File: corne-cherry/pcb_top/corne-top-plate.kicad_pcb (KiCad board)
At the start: 2 copper layers, 151.9 x 91.4 mm, 5 parts

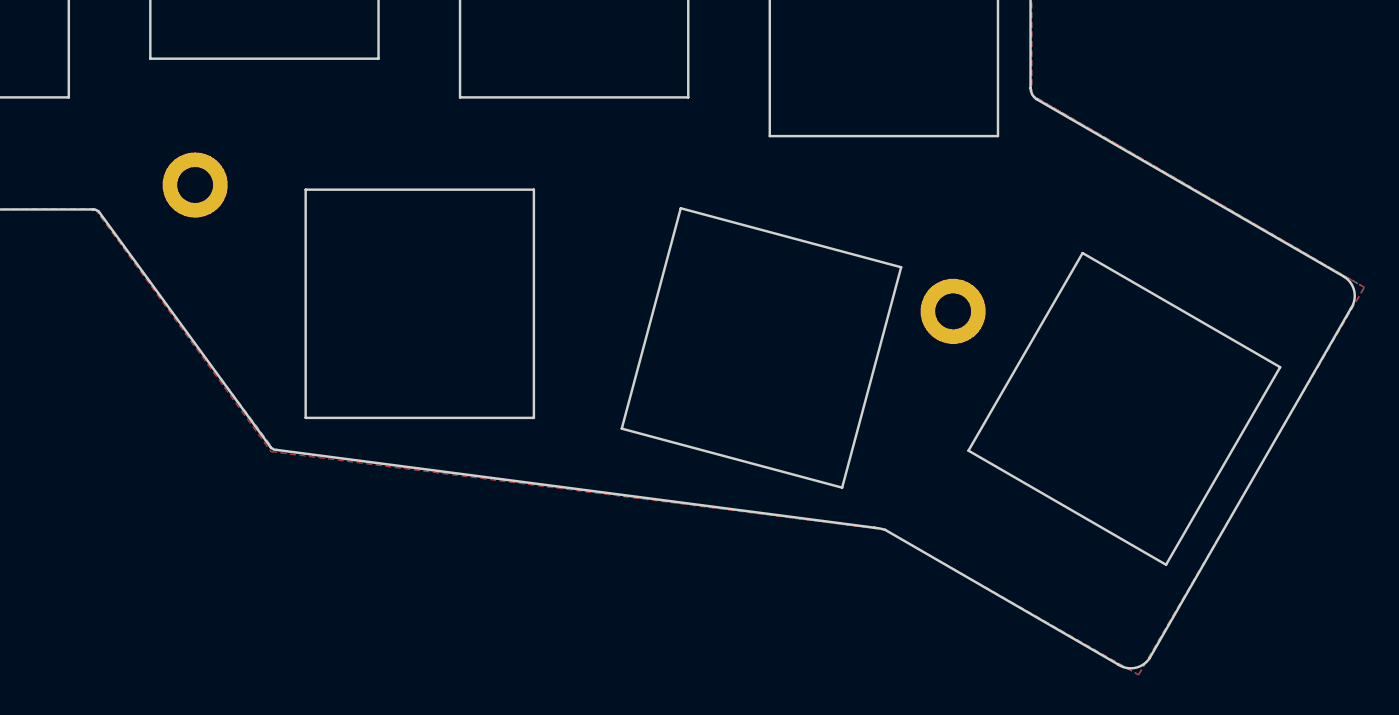
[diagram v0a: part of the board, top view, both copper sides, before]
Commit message: fixed outlines for pcb plates
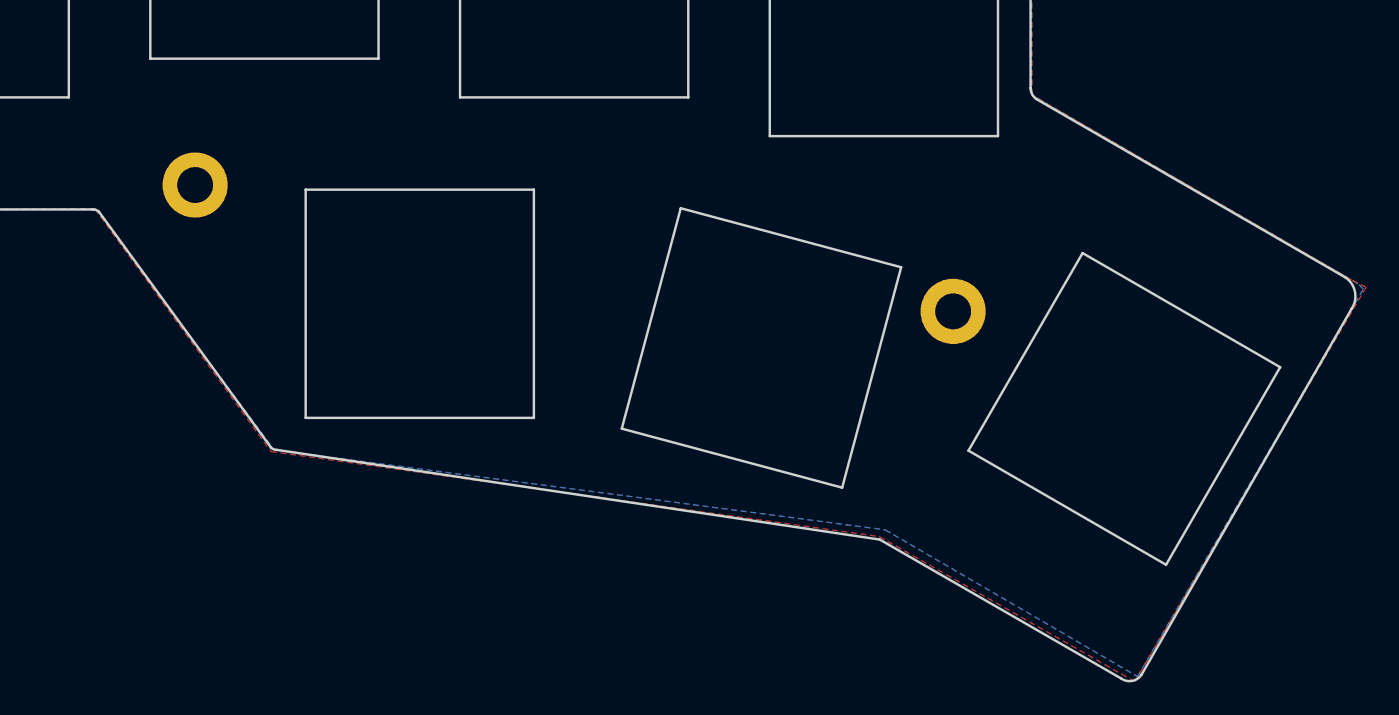
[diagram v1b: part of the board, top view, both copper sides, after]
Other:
- board size 151.9 x 91.4 mm -> 152 x 92.2 mm
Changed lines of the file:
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@@
-(kicad_pcb (version 20171130) (host pcbnew "(5.1.0)-1")
+(kicad_pcb (version 20171130) (host pcbnew "(5.1.8)-1")
   (general
     (thickness 1.6)
-    (drawings 137)
+    (drawings 136)
     (tracks 0)
     (zones 0)
@@
       (effects (font (size 1 1) (thickness 0.15)))
     )
-    (fp_text user %R (at 0.3 0) (layer F.Fab)
-      (effects (font (size 1 1) (thickness 0.15)))
-    )
-    (fp_circle (center 0 0) (end 2.2 0) (layer Cmts.User) (width 0.15))
-    (fp_circle (center 0 0) (end 2.45 0) (layer F.CrtYd) (width 0.05))
+    (fp_circle (center 0 0) (end 2.2 0) (layer Cmts.User) (width 0.15))
+    (fp_circle (center 0 0) (end 2.45 0) (layer F.CrtYd) (width 0.05))
+    (fp_text user %R (at 0.3 0) (layer F.Fab)
+      (effects (font (size 1 1) (thickness 0.15)))
+    )
     (pad "" thru_hole circle (at 0 0) (size 4 4) (drill 2.2) (layers *.Cu *.Mask))
   )
@@
       (effects (font (size 1 1) (thickness 0.15)))
     )
-    (fp_text user %R (at 0.3 0) (layer F.Fab)
-      (effects (font (size 1 1) (thickness 0.15)))
-    )
-    (fp_circle (center 0 0) (end 2.2 0) (layer Cmts.User) (width 0.15))
-    (fp_circle (center 0 0) (end 2.45 0) (layer F.CrtYd) (width 0.05))
+    (fp_circle (center 0 0) (end 2.2 0) (layer Cmts.User) (width 0.15))
+    (fp_circle (center 0 0) (end 2.45 0) (layer F.CrtYd) (width 0.05))
+    (fp_text user %R (at 0.3 0) (layer F.Fab)
+      (effects (font (size 1 1) (thickness 0.15)))
+    )
     (pad "" thru_hole circle (at 0 0) (size 4 4) (drill 2.2) (layers *.Cu *.Mask))
   )
@@
       (effects (font (size 1 1) (thickness 0.15)))
     )
-    (fp_text user %R (at 0.3 0) (layer F.Fab)
-      (effects (font (size 1 1) (thickness 0.15)))
-    )
-    (fp_circle (center 0 0) (end 2.2 0) (layer Cmts.User) (width 0.15))
-    (fp_circle (center 0 0) (end 2.45 0) (layer F.CrtYd) (width 0.05))
+    (fp_circle (center 0 0) (end 2.2 0) (layer Cmts.User) (width 0.15))
+    (fp_circle (center 0 0) (end 2.45 0) (layer F.CrtYd) (width 0.05))
+    (fp_text user %R (at 0.3 0) (layer F.Fab)
+      (effects (font (size 1 1) (thickness 0.15)))
+    )
     (pad "" thru_hole circle (at 0 0) (size 4 4) (drill 2.2) (layers *.Cu *.Mask))
   )
@@
       (effects (font (size 1 1) (thickness 0.15)))
     )
-    (fp_text user %R (at 0.3 0) (layer F.Fab)
-      (effects (font (size 1 1) (thickness 0.15)))
-    )
-    (fp_circle (center 0 0) (end 2.2 0) (layer Cmts.User) (width 0.15))
-    (fp_circle (center 0 0) (end 2.45 0) (layer F.CrtYd) (width 0.05))
+    (fp_circle (center 0 0) (end 2.2 0) (layer Cmts.User) (width 0.15))
+    (fp_circle (center 0 0) (end 2.45 0) (layer F.CrtYd) (width 0.05))
+    (fp_text user %R (at 0.3 0) (layer F.Fab)
+      (effects (font (size 1 1) (thickness 0.15)))
+    )
     (pad "" thru_hole circle (at 0 0) (size 4 4) (drill 2.2) (layers *.Cu *.Mask))
   )
@@
       (effects (font (size 1 1) (thickness 0.15)))
     )
-    (fp_text user %R (at 0.3 0) (layer F.Fab)
-      (effects (font (size 1 1) (thickness 0.15)))
-    )
-    (fp_circle (center 0 0) (end 2.2 0) (layer Cmts.User) (width 0.15))
-    (fp_circle (center 0 0) (end 2.45 0) (layer F.CrtYd) (width 0.05))
-    (pad "" thru_hole circle (at 0 0) (size 4 4) (drill 2.2) (layers *.Cu *.Mask))
-  )
+    (fp_circle (center 0 0) (end 2.2 0) (layer Cmts.User) (width 0.15))
+    (fp_circle (center 0 0) (end 2.45 0) (layer F.CrtYd) (width 0.05))
+    (fp_text user %R (at 0.3 0) (layer F.Fab)
+      (effects (font (size 1 1) (thickness 0.15)))
+    )
+    (pad "" thru_hole circle (at 0 0) (size 4 4) (drill 2.2) (layers *.Cu *.Mask))
+  )
+  (gr_line (start 180.8 152.8) (end 193.68968 130.34646) (angle 90) (layer Edge.Cuts) (width 0.15))
   (gr_line (start 44 98.375) (end 44 84.375) (layer Edge.Cuts) (width 0.15))
   (gr_line (start 44 98.375) (end 58 98.375) (layer Edge.Cuts) (width 0.15))
@@
   (gr_line (start 63 70.125) (end 77 70.125) (layer Edge.Cuts) (width 0.15))
   (gr_arc (start 174.847282 116.785192) (end 173.997282 116.810192) (angle -52.52752939) (layer Edge.Cuts) (width 0.15))
-  (gr_arc (start 192.500001 129.550001) (end 193.65 130.325) (angle -90.22347501) (layer Edge.Cuts) (width 0.15))
-  (gr_line (start 193.270509 128.396988) (end 174.35 117.475) (layer Edge.Cuts) (width 0.15))
+  (gr_arc (start 192.539681 129.571461) (end 193.68968 130.34646) (angle -90.22347501) (layer Edge.Cuts) (width 0.15))
+  (gr_line (start 193.310189 128.418448) (end 174.35 117.475) (layer Edge.Cuts) (width 0.15))
   (gr_line (start 63 84.125) (end 63 70.125) (layer Edge.Cuts) (width 0.15))
   (gr_line (start 77 70.125) (end 77 84.125) (layer Edge.Cuts) (width 0.15))
-  (gr_arc (start 180.14425 151.010957) (end 179.369251 152.160956) (angle -90.22347501) (layer Edge.Cuts) (width 0.15))
-  (gr_arc (start 164.087404 147.16844) (end 165.075 143.9) (angle -11.21335546) (layer Edge.Cuts) (width 0.15))
-  (gr_line (start 181.297263 151.781465) (end 193.65 130.325) (layer Edge.Cuts) (width 0.15))
-  (gr_line (start 165.075 143.9) (end 179.369251 152.160956) (layer Edge.Cuts) (width 0.15))
-  (gr_line (start 127.75 139) (end 164.420556 143.770344) (layer Edge.Cuts) (width 0.15))
-  (gr_arc (start 127.75 138.5) (end 127.75 139) (angle 45) (layer Edge.Cuts) (width 0.15))
-  (gr_line (start 116.853553 124.396447) (end 127.396447 138.853553) (angle 90) (layer Edge.Cuts) (width 0.15))
+  (gr_arc (start 127.753553 138.496447) (end 127.753553 138.996447) (angle 45) (layer Edge.Cuts) (width 0.15))
+  (gr_line (start 116.853553 124.396447) (end 127.4 138.85) (angle 90) (layer Edge.Cuts) (width 0.15))
   (gr_line (start 169.26 130.5) (end 169.25 130.5) (angle 90) (layer Eco2.User) (width 2.5))
   (gr_line (start 122.76 122.75) (end 122.75 122.75) (angle 90) (layer Eco2.User) (width 2.5))
@@
   (gr_line (start 174 66.25) (end 173.997282 116.810192) (angle 90) (layer Edge.Cuts) (width 0.15))
   (gr_arc (start 173.5 66.25) (end 173.5 65.75) (angle 90) (layer Edge.Cuts) (width 0.15))
-  (gr_arc (start 116.5 124.75) (end 116.5 124.25) (angle 45) (layer Edge.Cuts) (width 0.15))
   (gr_arc (start 61.5 68.5) (end 61 68.5) (angle 90) (layer Edge.Cuts) (width 0.15))
   (gr_arc (start 98.5 67.5) (end 99 67.5) (angle 90) (layer Edge.Cuts) (width 0.15))
@@
   (gr_arc (start 60.4996 101.1603) (end 60.4996 100.6603) (angle 90) (layer Edge.Cuts) (width 0.15))
   (gr_arc (start 60.5043 81.75) (end 61.0043 81.75) (angle 90) (layer Edge.Cuts) (width 0.15))
+  (gr_arc (start 180.07 152.3) (end 180.8 152.8) (angle 90) (layer Edge.Cuts) (width 0.15))
+  (gr_arc (start 116.5 124.75) (end 116.5 124.25) (angle 45) (layer Edge.Cuts) (width 0.15))
+  (gr_line (start 164.75 144.5) (end 179.57 153.03) (angle 90) (layer Edge.Cuts) (width 0.15))
+  (gr_line (start 127.753553 138.996447) (end 164.75 144.5) (angle 90) (layer Edge.Cuts) (width 0.15))
   (zone (net 0) (net_name "") (layer B.Cu) (hatch edge 0.508)
     (connect_pads (clearance 0.508))
@@
         (xy 98.9 67.9) (xy 60.7 68) (xy 60.750702 81.875) (xy 41.5 81.875) (xy 41.5 100.875)
         (xy 60.816942 100.875638) (xy 60.9 124.7) (xy 116.6 124.2) (xy 127.6 139) (xy 165.075 143.9)
-        (xy 180.625 152.8) (xy 194.475 129.025) (xy 194.075 128.8)
+        (xy 180.562 152.9045) (xy 194.412 129.1295) (xy 194.075 128.8)
       )
     )
@@
         (xy 136 63.2) (xy 136 60.9) (xy 118 60.9) (xy 118 63.2) (xy 98.8 63.2)
         (xy 98.9 67.9) (xy 60.7 68) (xy 60.748938 81.874121) (xy 41.5 81.875) (xy 41.5 100.875)
-        (xy 60.815963 100.875649) (xy 60.9 124.7) (xy 116.6 124.2) (xy 127.4 139.1) (xy 165.05 143.9)
-        (xy 180.625 152.8) (xy 194.475 129.025) (xy 193.7 128.575)
+        (xy 60.815963 100.875649) (xy 60.9 124.7) (xy 116.6 124.2) (xy 127.4 139.1) (xy 164.7135 144.314)
+        (xy 180.39375 153.214) (xy 194.58025 129.025) (xy 193.7 128.575)
       )
     )
